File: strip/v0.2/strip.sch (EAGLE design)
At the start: 99 parts, among them IC1 LP2992, IC2 AUIRS2184S, IC3 MAX3051, IC4 OPA335, IC5 AUIRS2184S, IC6 AUIRS2184S, IC7 STM32F050CX, Q1 IRF7828, Q2 IRF7828, Q3 IRF7828, Q4 IRF7828, Q5 IRF7828, Q6 IRF7828

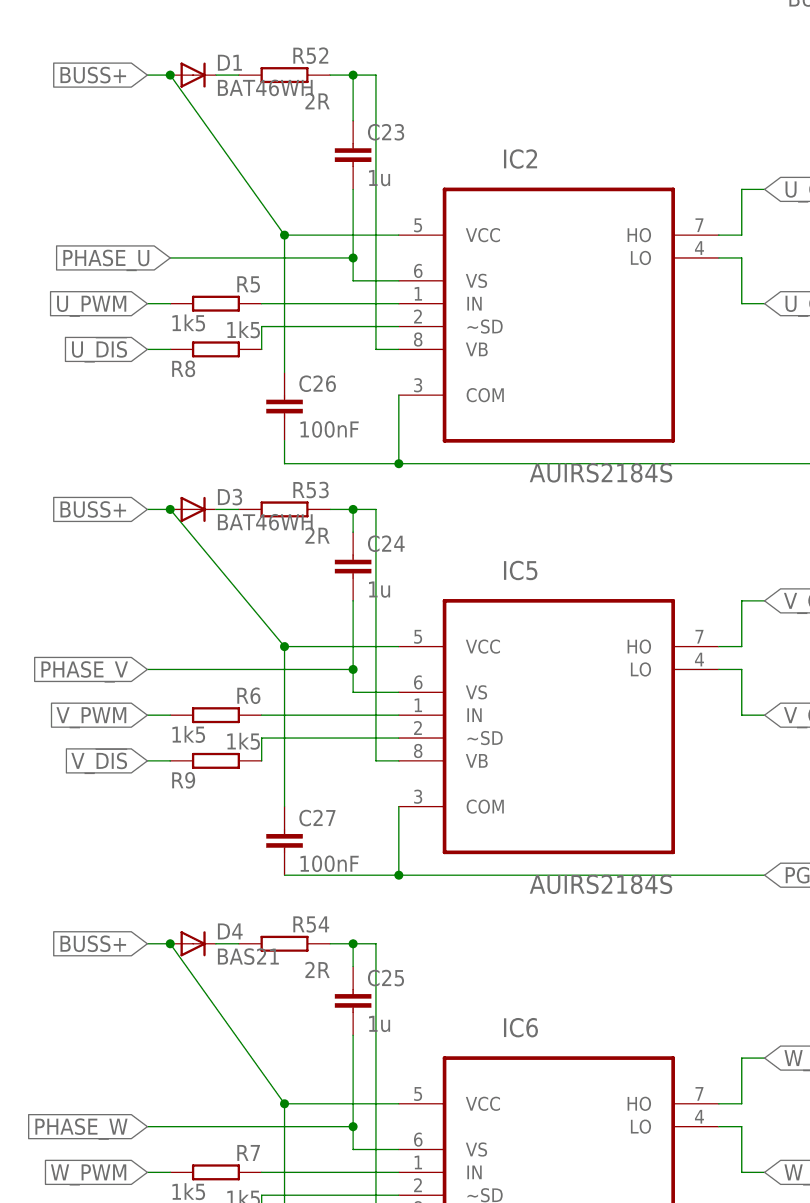
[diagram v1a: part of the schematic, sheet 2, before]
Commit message: Updated bootstrap circuit
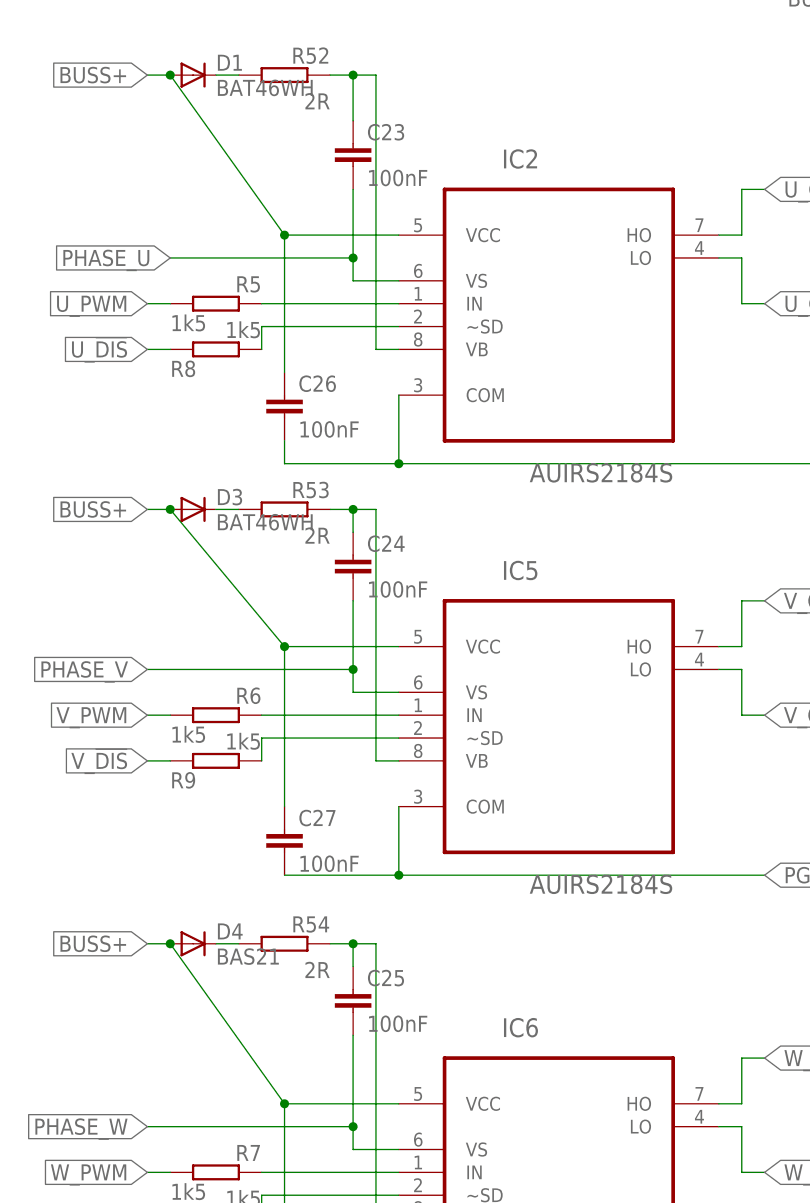
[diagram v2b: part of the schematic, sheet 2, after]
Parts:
- C23, C24, C25: value 1u -> 100nF
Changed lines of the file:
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@@
 <grid distance="0.1" unitdist="inch" unit="inch" style="lines" multiple="1" display="no" altdistance="0.01" altunitdist="inch" altunit="inch"/>
 <layers>
-<layer number="1" name="Top" color="4" fill="1" visible="yes" active="no"/>
-<layer number="2" name="Route2" color="1" fill="3" visible="yes" active="no"/>
-<layer number="3" name="Route3" color="4" fill="3" visible="yes" active="no"/>
-<layer number="4" name="Route4" color="1" fill="4" visible="yes" active="no"/>
-<layer number="5" name="Route5" color="4" fill="4" visible="yes" active="no"/>
-<layer number="6" name="Route6" color="1" fill="8" visible="yes" active="no"/>
-<layer number="7" name="Route7" color="4" fill="8" visible="yes" active="no"/>
-<layer number="8" name="Route8" color="1" fill="2" visible="yes" active="no"/>
-<layer number="9" name="Route9" color="4" fill="2" visible="yes" active="no"/>
-<layer number="10" name="Route10" color="1" fill="7" visible="yes" active="no"/>
-<layer number="11" name="Route11" color="4" fill="7" visible="yes" active="no"/>
-<layer number="12" name="Route12" color="1" fill="5" visible="yes" active="no"/>
-<layer number="13" name="Route13" color="4" fill="5" visible="yes" active="no"/>
-<layer number="14" name="Route14" color="1" fill="6" visible="yes" active="no"/>
-<layer number="15" name="Route15" color="4" fill="6" visible="yes" active="no"/>
-<layer number="16" name="Bottom" color="1" fill="1" visible="yes" active="no"/>
-<layer number="17" name="Pads" color="2" fill="1" visible="yes" active="no"/>
-<layer number="18" name="Vias" color="2" fill="1" visible="yes" active="no"/>
-<layer number="19" name="Unrouted" color="6" fill="1" visible="yes" active="no"/>
-<layer number="20" name="Dimension" color="15" fill="1" visible="yes" active="no"/>
-<layer number="21" name="tPlace" color="7" fill="1" visible="yes" active="no"/>
-<layer number="22" name="bPlace" color="7" fill="1" visible="yes" active="no"/>
-<layer number="23" name="tOrigins" color="15" fill="1" visible="yes" active="no"/>
-<layer number="24" name="bOrigins" color="15" fill="1" visible="yes" active="no"/>
-<layer number="25" name="tNames" color="7" fill="1" visible="yes" active="no"/>
-<layer number="26" name="bNames" color="7" fill="1" visible="yes" active="no"/>
-<layer number="27" name="tValues" color="7" fill="1" visible="yes" active="no"/>
-<layer number="28" name="bValues" color="7" fill="1" visible="yes" active="no"/>
+<layer number="1" name="Top" color="4" fill="1" visible="no" active="no"/>
+<layer number="2" name="Route2" color="1" fill="3" visible="no" active="no"/>
+<layer number="3" name="Route3" color="4" fill="3" visible="no" active="no"/>
+<layer number="4" name="Route4" color="1" fill="4" visible="no" active="no"/>
+<layer number="5" name="Route5" color="4" fill="4" visible="no" active="no"/>
+<layer number="6" name="Route6" color="1" fill="8" visible="no" active="no"/>
+<layer number="7" name="Route7" color="4" fill="8" visible="no" active="no"/>
+<layer number="8" name="Route8" color="1" fill="2" visible="no" active="no"/>
+<layer number="9" name="Route9" color="4" fill="2" visible="no" active="no"/>
+<layer number="10" name="Route10" color="1" fill="7" visible="no" active="no"/>
+<layer number="11" name="Route11" color="4" fill="7" visible="no" active="no"/>
+<layer number="12" name="Route12" color="1" fill="5" visible="no" active="no"/>
+<layer number="13" name="Route13" color="4" fill="5" visible="no" active="no"/>
+<layer number="14" name="Route14" color="1" fill="6" visible="no" active="no"/>
+<layer number="15" name="Route15" color="4" fill="6" visible="no" active="no"/>
+<layer number="16" name="Bottom" color="1" fill="1" visible="no" active="no"/>
+<layer number="17" name="Pads" color="2" fill="1" visible="no" active="no"/>
+<layer number="18" name="Vias" color="2" fill="1" visible="no" active="no"/>
+<layer number="19" name="Unrouted" color="6" fill="1" visible="no" active="no"/>
+<layer number="20" name="Dimension" color="15" fill="1" visible="no" active="no"/>
+<layer number="21" name="tPlace" color="7" fill="1" visible="no" active="no"/>
+<layer number="22" name="bPlace" color="7" fill="1" visible="no" active="no"/>
+<layer number="23" name="tOrigins" color="15" fill="1" visible="no" active="no"/>
+<layer number="24" name="bOrigins" color="15" fill="1" visible="no" active="no"/>
+<layer number="25" name="tNames" color="7" fill="1" visible="no" active="no"/>
+<layer number="26" name="bNames" color="7" fill="1" visible="no" active="no"/>
+<layer number="27" name="tValues" color="7" fill="1" visible="no" active="no"/>
+<layer number="28" name="bValues" color="7" fill="1" visible="no" active="no"/>
 <layer number="29" name="tStop" color="7" fill="3" visible="no" active="no"/>
 <layer number="30" name="bStop" color="7" fill="6" visible="no" active="no"/>
@@
 <layer number="35" name="tGlue" color="7" fill="4" visible="no" active="no"/>
 <layer number="36" name="bGlue" color="7" fill="5" visible="no" active="no"/>
-<layer number="37" name="tTest" color="7" fill="1" visible="yes" active="no"/>
-<layer number="38" name="bTest" color="7" fill="1" visible="yes" active="no"/>
+<layer number="37" name="tTest" color="7" fill="1" visible="no" active="no"/>
+<layer number="38" name="bTest" color="7" fill="1" visible="no" active="no"/>
 <layer number="39" name="tKeepout" color="4" fill="11" visible="no" active="no"/>
 <layer number="40" name="bKeepout" color="1" fill="11" visible="no" active="no"/>
@@
 <layer number="44" name="Drills" color="7" fill="1" visible="no" active="no"/>
 <layer number="45" name="Holes" color="7" fill="1" visible="no" active="no"/>
-<layer number="46" name="Milling" color="3" fill="1" visible="yes" active="no"/>
-<layer number="47" name="Measures" color="7" fill="1" visible="yes" active="no"/>
-<layer number="48" name="Document" color="7" fill="1" visible="yes" active="no"/>
-<layer number="49" name="Reference" color="7" fill="1" visible="yes" active="no"/>
-<layer number="50" name="dxf" color="7" fill="1" visible="yes" active="no"/>
-<layer number="51" name="tDocu" color="7" fill="1" visible="yes" active="no"/>
-<layer number="52" name="bDocu" color="7" fill="1" visible="yes" active="no"/>
-<layer number="53" name="tGND_GNDA" color="7" fill="9" visible="yes" active="no"/>
-<layer number="54" name="bGND_GNDA" color="1" fill="9" visible="yes" active="no"/>
-<layer number="56" name="wert" color="7" fill="1" visible="yes" active="no"/>
-<layer number="59" name="Invisible" color="7" fill="1" visible="yes" active="no"/>
-<layer number="61" name="stand" color="7" fill="1" visible="yes" active="no"/>
+<layer number="46" name="Milling" color="3" fill="1" visible="no" active="no"/>
+<layer number="47" name="Measures" color="7" fill="1" visible="no" active="no"/>
+<layer number="48" name="Document" color="7" fill="1" visible="no" active="no"/>
+<layer number="49" name="Reference" color="7" fill="1" visible="no" active="no"/>
+<layer number="50" name="dxf" color="7" fill="1" visible="no" active="no"/>
+<layer number="51" name="tDocu" color="7" fill="1" visible="no" active="no"/>
+<layer number="52" name="bDocu" color="7" fill="1" visible="no" active="no"/>
+<layer number="53" name="tGND_GNDA" color="7" fill="9" visible="no" active="no"/>
+<layer number="54" name="bGND_GNDA" color="1" fill="9" visible="no" active="no"/>
+<layer number="56" name="wert" color="7" fill="1" visible="no" active="no"/>
+<layer number="59" name="Invisible" color="7" fill="1" visible="no" active="no"/>
+<layer number="61" name="stand" color="7" fill="1" visible="no" active="no"/>
 <layer number="91" name="Nets" color="2" fill="1" visible="yes" active="yes"/>
 <layer number="92" name="Busses" color="1" fill="1" visible="yes" active="yes"/>
@@
 <attribute name="PARTNO" value="*"/>
 </part>
-<part name="C23" library="pel_dipol_comp" deviceset="CAPACITOR" device="-0603" value="1u">
+<part name="C23" library="pel_dipol_comp" deviceset="CAPACITOR" device="-0603" value="100nF">
 <attribute name="PARTNO" value="cap-tan-0603-1u"/>
 </part>
@@
 <attribute name="PARTNO" value="*"/>
 </part>
-<part name="C24" library="pel_dipol_comp" deviceset="CAPACITOR" device="-0603" value="1u">
+<part name="C24" library="pel_dipol_comp" deviceset="CAPACITOR" device="-0603" value="100nF">
 <attribute name="PARTNO" value="cap-tan-0603-1u"/>
 </part>
@@
 <attribute name="PARTNO" value="*"/>
 </part>
-<part name="C25" library="pel_dipol_comp" deviceset="CAPACITOR" device="-0603" value="1u">
+<part name="C25" library="pel_dipol_comp" deviceset="CAPACITOR" device="-0603" value="100nF">
 <attribute name="PARTNO" value="cap-tan-0603-1u"/>
 </part>

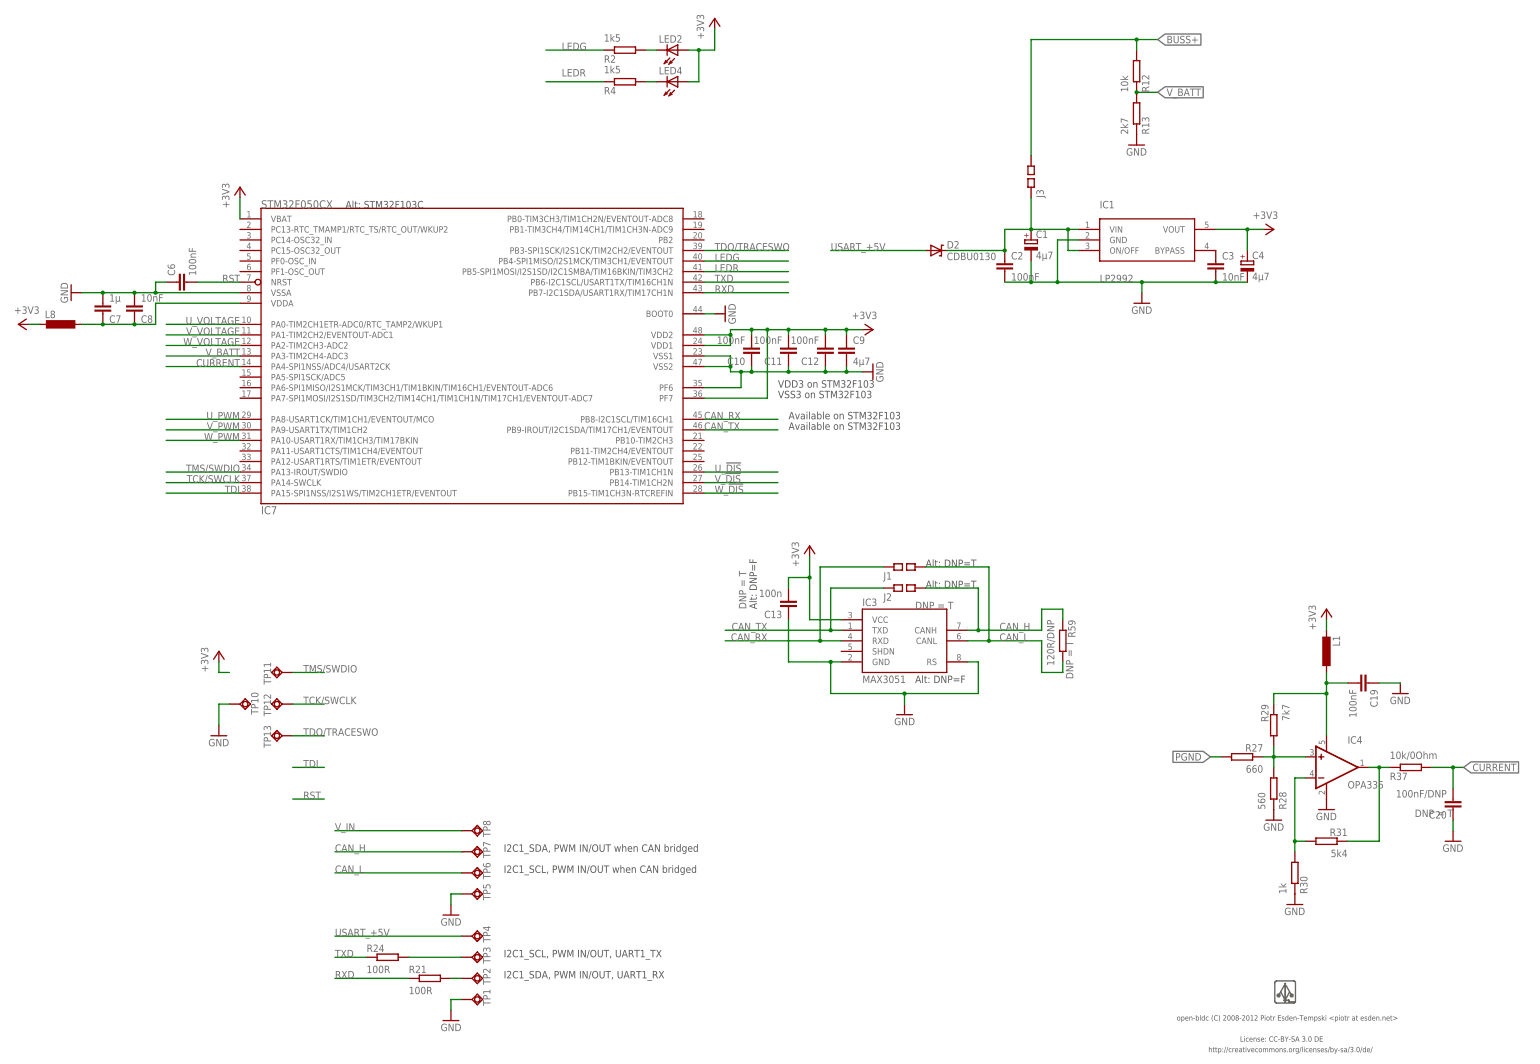
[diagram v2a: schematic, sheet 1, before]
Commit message: Updated current measurement circuit.
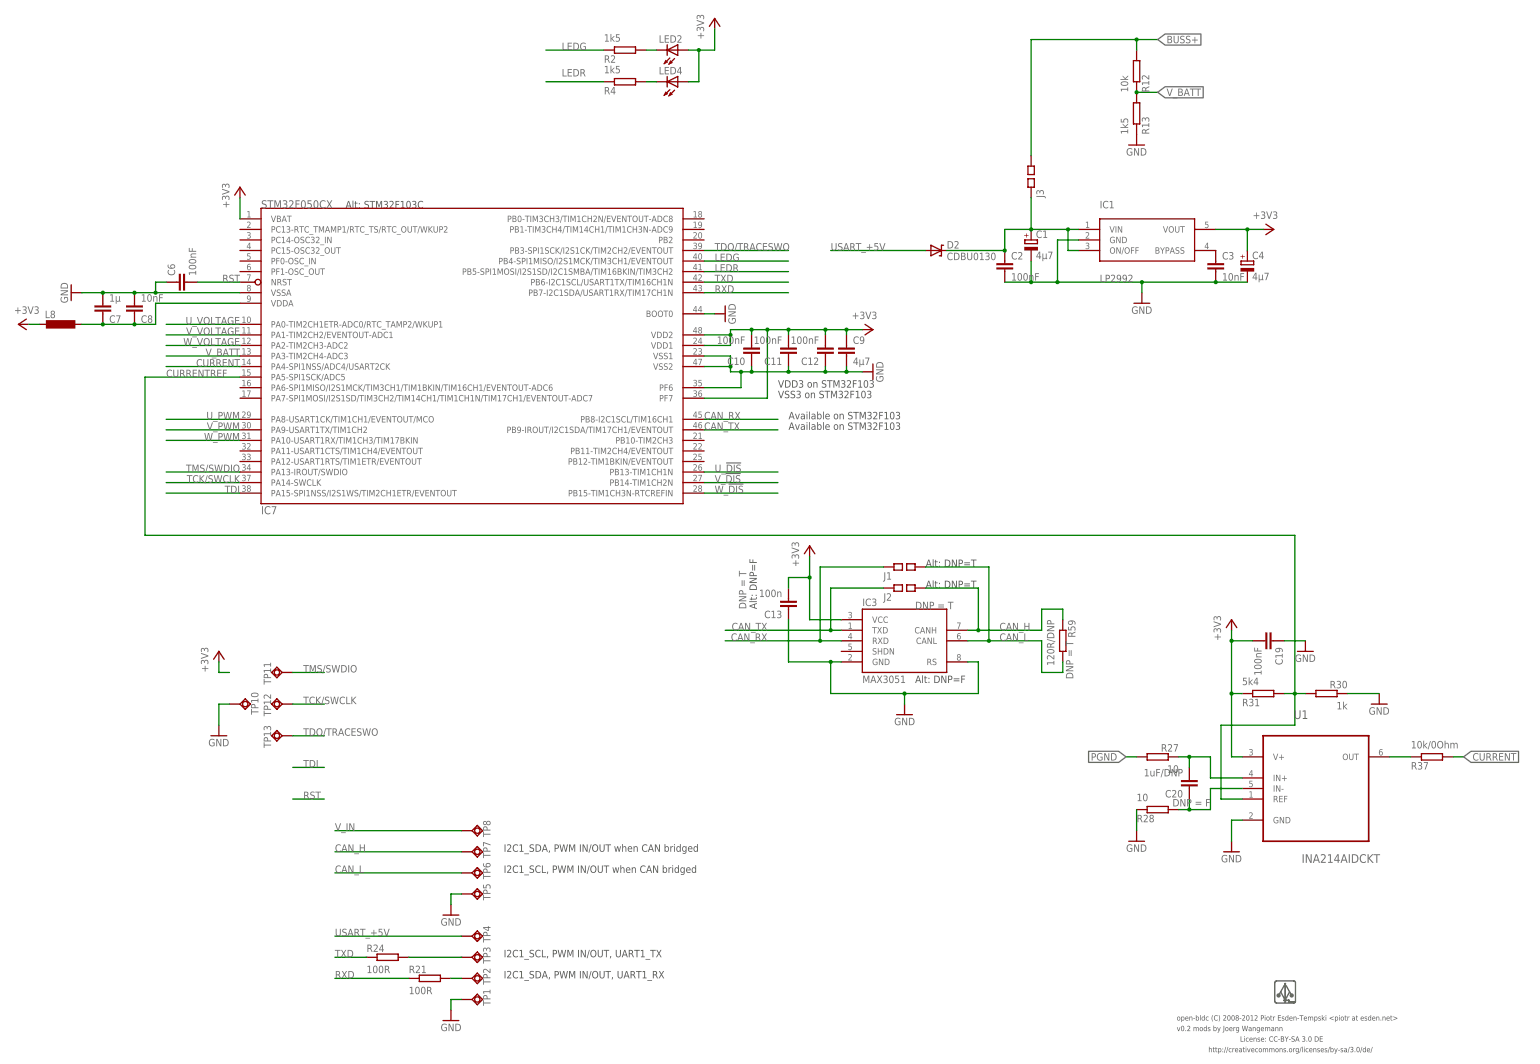
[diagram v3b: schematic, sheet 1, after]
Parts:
- removed IC4: OPA335, open-bldc:OPA335
- removed L1: INDUCTOR-0603, res_cap:INDUCTOR-0603
- removed R29: 7k7, pel_dipol_comp:RESISTOR-0402
- added U1: INA214AIDCKT, open-bldc:INA214AIDCKT
- C20: value 100nF/DNP -> 1uF/DNP; device pel_dipol_comp:CAPACITOR-0402 -> pel_dipol_comp:CAPACITOR-0603; DNP T -> F
- R13: value 2k7 -> 1k5; PARTNO res-0402-2k7 -> res-0402-1k5
- R27: value 660 -> 10
- R28: value 560 -> 10
- R45: value 0.005Ohm -> 0.002Ohm
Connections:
- removed net N$11: IC4.+IN, R27.1, R28.2, R29.2
- removed net N$12: IC4.-IN, R30.2, R31.2
- removed net N$9: C19.2, IC4.V+, L1.1, R29.1
- new net CURRENTREF: IC7.PA5-SPI1SCK/ADC5, R30.2, R31.2, U1.REF
- new net INA21_INN: C20.1, R28.2, U1.IN-
- new net INA21_INP: C20.2, R27.1, U1.IN+
- net +3V3: now also C19.2, R31.1, U1.V+; no longer L1.2
- net CURRENT: no longer C20.2
- net CURRENT_RAW: now also U1.OUT; no longer IC4.OUT, R31.1
- net GND: now also U1.GND; no longer C20.1, IC4.V-
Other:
- note added: "v0.2 mods by Joerg Wangemann"
- moved on the sheet: C19, C20, R27, R28, R30, R31, R37
